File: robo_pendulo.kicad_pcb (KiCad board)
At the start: 2 copper layers, 50 parts, among them J1 Conn_01x02, J2 Conn_01x09, J3 Conn_01x02_Male, J4 Conn_01x02_Male, J5 Conn_01x02_Male, J6 Conn_01x02_Male, J7 Conn_01x04, J8 Conn_01x04, J9 Conn_02x13_Odd_Even, SW1 SW_SPST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

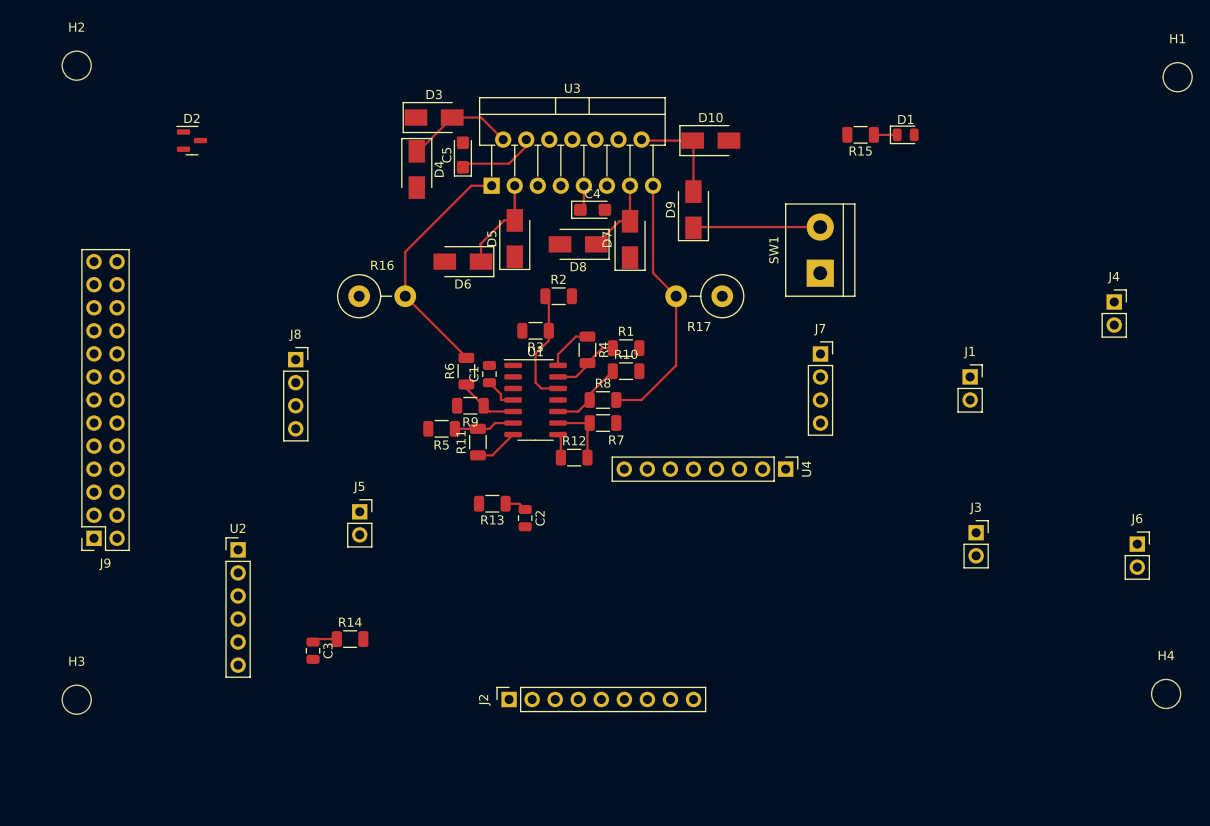
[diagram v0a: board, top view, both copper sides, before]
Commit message: Adjust board layout
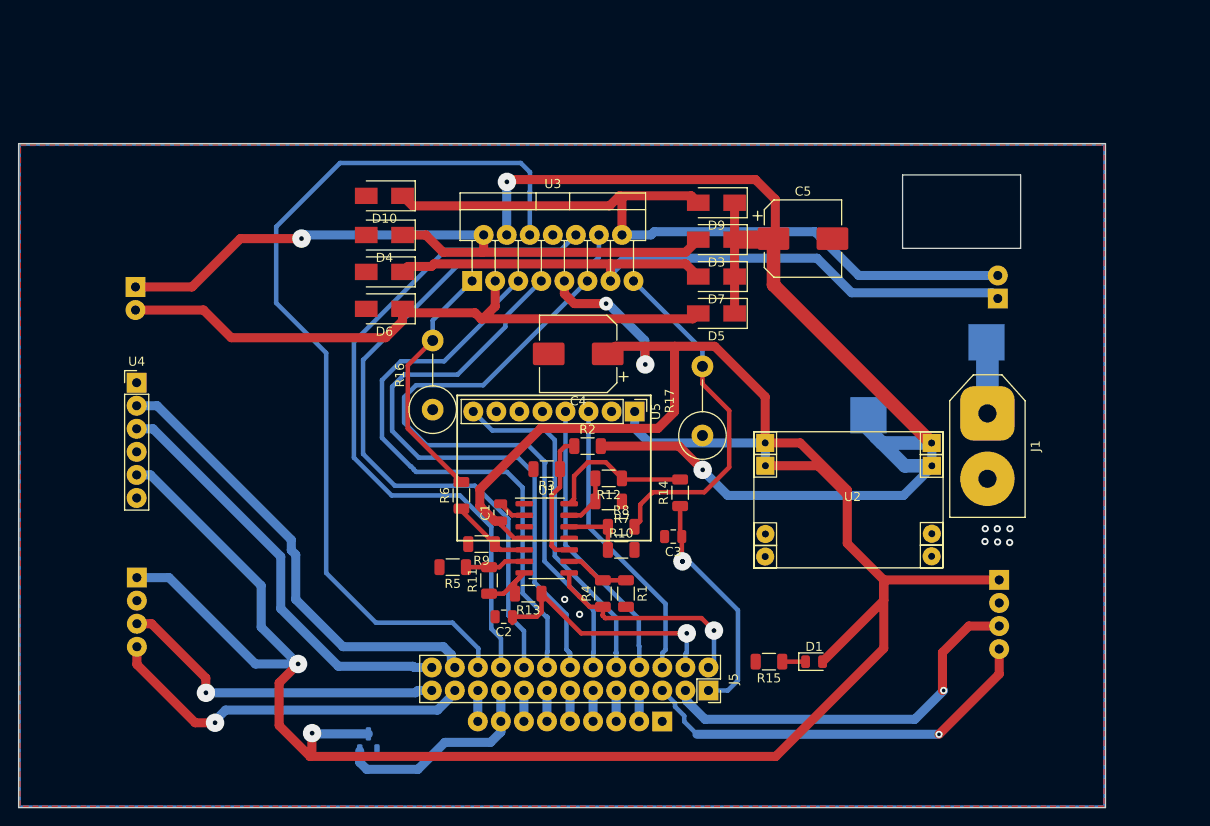
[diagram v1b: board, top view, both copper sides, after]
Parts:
- removed H1, H2, H3, H4: MountingHole, MountingHole:MountingHole_3.2mm_M3
- removed the J3 at (168.9, 88.3)
- removed the J4 at (184.2, 62.9)
- removed the J5 at (101.0, 86.0)
- removed SW1: SW_SPST, TerminalBlock:TerminalBlock_bornier-2_P5.08mm
- added ?: , , F.Cu at (157.1, 75.3)
- added ?: , , F.Cu at (170.1, 67.3)
- added J7: Conn_01x02, Connector_PinHeader_2.54mm:PinHeader_1x02_P2.54mm_Vertical, B.Cu at (171.3, 62.5)
- added U2: mini-DC-DC, dc-dc-converter:mini-DC-DC, F.Cu at (154.9, 83.8)
- C4, C5: footprint Capacitor_Tantalum_SMD:CP_EIA-3216-12_Kemet-S -> Capacitor_SMD:CP_Elec_8x10
- D2, J2: moved to B.Cu
- J1: footprint Connector_PinSocket_2.54mm:PinSocket_1x02_P2.54mm_Vertical -> Connector_AMASS:AMASS_XT60-M_1x02_P7.20mm_Vertical
- J3: renamed from J7; moved to B.Cu
- J4: renamed from J8; moved to B.Cu
- J6: value Conn_01x02_Male -> Conn_01x02; footprint Connector_PinSocket_2.54mm:PinSocket_1x02_P2.54mm_Vertical -> Connector_PinHeader_2.54mm:PinHeader_1x02_P2.54mm_Vertical; moved to B.Cu
- R16, R17: footprint Resistor_THT:R_Axial_DIN0414_L11.9mm_D4.5mm_P5.08mm_Vertical -> Resistor_THT:R_Axial_DIN0516_L15.5mm_D5.0mm_P7.62mm_Vertical
- moved J6 113.9 mm to (76.3, 61.2), turned to 180 degrees
- moved J5 69.7 mm to (139.4, 105.7), turned to -90 degrees
- moved D2 69.1 mm to (102.0, 111.4), turned to 90 degrees
- moved D1 58.9 mm to (151.1, 102.5)
- moved R15 58.9 mm to (146.1, 102.5)
- moved C3 41.6 mm to (135.6, 88.7), turned to 180 degrees
- moved R14 39.8 mm to (136.3, 83.9), turned to 90 degrees
- moved C5 38.6 mm to (149.9, 55.9), turned to 0 degrees
- moved D10 36.5 mm to (103.7, 51.2), turned to 180 degrees
- moved D3 33.9 mm to (140.3, 56.0), turned to 180 degrees
- moved J3 31.7 mm to (171.5, 93.5), turned to 180 degrees
- moved J4 29.7 mm to (76.5, 93.2), turned to 180 degrees
- moved R1 27.0 mm to (130.4, 95.0), turned to -90 degrees
- moved R4 26.9 mm to (127.8, 95.0), turned to 90 degrees
- moved D5 23.7 mm to (140.3, 64.1), turned to 180 degrees
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- renumbered J9 to J5, U2 to U4, U4 to U5
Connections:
- D2 pad 1: Net-(D2-Pad1) -> (no net)
- D2 pad 2: +5V -> 5V_OUT
- D2 pad 3: (no net) -> +5V
- J1 pad 1: +BATT -> /BATT_IN
- J2 pad 1: CLP -> GND
- J2 pad 2: +5V -> NEAR
- J2 pad 3: SS1 -> SS5
- J2 pad 4: SS2 -> SS4
- J2 pad 6: SS4 -> SS2
- J2 pad 7: SS5 -> SS1
- J2 pad 8: NEAR -> 5V_OUT
- J2 pad 9: GND -> CLP
- J5 pad 1: unconnected-(J9-Pad1) -> MEAS_RM
- J5 pad 10: unconnected-(J9-Pad10) -> IMU_INT
- J5 pad 11: unconnected-(J9-Pad11) -> SS4
- J5 pad 12: unconnected-(J9-Pad12) -> MOT_ENB
- J5 pad 13: unconnected-(J9-Pad13) -> SS3
- J5 pad 14: unconnected-(J9-Pad14) -> MOT_IN2
- J5 pad 15: unconnected-(J9-Pad15) -> SS2
- J5 pad 16: unconnected-(J9-Pad16) -> MOT_IN1
- J5 pad 17: unconnected-(J9-Pad17) -> SS1
- J5 pad 18: unconnected-(J9-Pad18) -> MOT_IN4
- J5 pad 19: unconnected-(J9-Pad19) -> 5V_OUT
- J5 pad 2: unconnected-(J9-Pad2) -> MEAS_BATT
- J5 pad 20: unconnected-(J9-Pad20) -> MOT_IN3
- J5 pad 21: unconnected-(J9-Pad21) -> CLP
- J5 pad 22: unconnected-(J9-Pad22) -> MOT_ENA
- J5 pad 23: unconnected-(J9-Pad23) -> ENC1_B
- J5 pad 24: unconnected-(J9-Pad24) -> RXB
- J5 pad 25: unconnected-(J9-Pad25) -> ENC1_A
- J5 pad 26: unconnected-(J9-Pad26) -> TXB
- J5 pad 3: unconnected-(J9-Pad3) -> ENC0_A
- J5 pad 4: unconnected-(J9-Pad4) -> MEAS_LM
- J5 pad 5: unconnected-(J9-Pad5) -> ENC0_B
- J5 pad 6: unconnected-(J9-Pad6) -> IMU_SCL
- J5 pad 7: unconnected-(J9-Pad7) -> NEAR
- J5 pad 8: Net-(D2-Pad1) -> IMU_SDA
- J5 pad 9: unconnected-(J9-Pad9) -> SS5
- J6 pad 1: GND -> MOT_OUT1
- J6 pad 2: GND -> MOT_OUT2
- R10 pad 1: Net-(R8-Pad1) -> Net-(R10-Pad1)
- R16 pad 2: /CURR_RM -> /CURR_LM
- R17 pad 2: /CURR_LM -> /CURR_RM
- R6 pad 2: /CURR_RM -> /CURR_LM
- R8 pad 1: Net-(R8-Pad1) -> Net-(R10-Pad1)
- R8 pad 2: /CURR_LM -> /CURR_RM
- U1 pad 10: Net-(R8-Pad1) -> Net-(R2-Pad1)
- U1 pad 12: Net-(R2-Pad1) -> Net-(R10-Pad1)
- U1 pad 13: Net-(R1-Pad1) -> Net-(R12-Pad2)
- U1 pad 14: MEAS_BATT -> Net-(R12-Pad1)
- U1 pad 8: Net-(R12-Pad1) -> MEAS_BATT
- U1 pad 9: Net-(R12-Pad2) -> Net-(R1-Pad1)
- U3 pad 1: /CURR_RM -> /CURR_LM
- U3 pad 15: /CURR_LM -> /CURR_RM
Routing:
- net +5V: track 6.42 -> 308.2 mm, vias 0 -> 4
- net +BATT: track 22.5 -> 146.5 mm, vias 0 -> 2
- net MOT_ENA: track 0.00 -> 100.9 mm
- net MOT_IN4: track 0.00 -> 79.5 mm
- net MOT_IN3: track 0.00 -> 76.3 mm
- net MOT_OUT3: track 8.69 -> 81.5 mm
- net MOT_OUT4: track 11.3 -> 82.2 mm
- net MOT_ENB: track 0.00 -> 70.7 mm
- net MOT_IN2: track 0.00 -> 67.5 mm
- net MOT_IN1: track 0.00 -> 65.4 mm
- net MOT_OUT1: track 12.1 -> 76.8 mm, vias 0 -> 1
- net MOT_OUT2: track 10.8 -> 71.1 mm
- net RXB: track 0.00 -> 51.1 mm
- net TXB: track 0.00 -> 46.8 mm
- net ENC0_B: track 0.00 -> 45.2 mm, vias 0 -> 1
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- added copper zone on B.Cu, net GND
- added copper zone on F.Cu, net GND
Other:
- board outline added: 119.7 x 73.2 mm
